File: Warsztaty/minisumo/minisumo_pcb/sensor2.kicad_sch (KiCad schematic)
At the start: 1 part

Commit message: chyba gotowy schemat
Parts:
- removed SPI1: MTSW-103-23-F-D-230, MTSW-103-23-F-D-230:SAMTEC_MTSW-103-23-F-D-230, symbol MTSW-103-23-F-D-230:MTSW-103-23-F-D-230
- added SPI3: MTSW-103-23-F-D-230, MTSW-103-23-F-D-230:SAMTEC_MTSW-103-23-F-D-230, symbol MTSW-103-23-F-D-230:MTSW-103-23-F-D-230
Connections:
- net +5V: now also SPI3.02
- net GND: now also SPI3.01
- new net G2: SPI3.06
- new net SCL: SPI3.04
- new net SDA: SPI3.03
- new net X2: SPI3.05
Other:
- note added: "Sensor2"
- note removed: "Programming connector"

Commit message: stan przed usunięciem jednego czujnika lini
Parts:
- added R3: 20k, Resistor_SMD:R_0805_2012Metric, symbol Device:R_Small
- added R6: 10k, Resistor_SMD:R_0805_2012Metric, symbol Device:R_Small
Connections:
- net GND: now also R3.1
- net X2: now also R3.2, R6.2; no longer SPI3.05
- new net: R6.1, SPI3.05

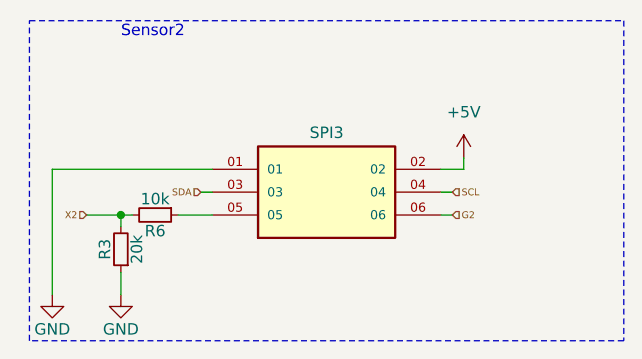
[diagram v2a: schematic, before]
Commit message: Wstępny wyglad robota i płytki
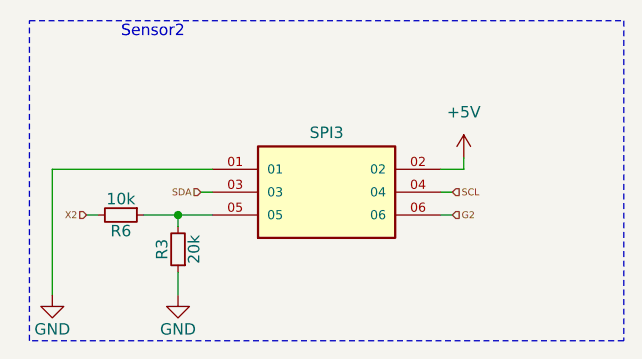
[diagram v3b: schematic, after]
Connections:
- net X2: no longer R3.2
- net at R6.1, SPI3.05: now also R3.2
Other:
- moved on the sheet: R3, R6
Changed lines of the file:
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@@
 	(paper "A4")
 	(junction
-		(at 25.4 35.56)
+		(at 31.75 35.56)
 		(diameter 0)
 		(color 0 0 0 0)
@@
 	(wire
 		(pts
-			(xy 25.4 35.56) (xy 25.4 36.83)
-		)
-		(stroke
-			(width 0)
-			(type default)
-		)
-	)
-	(wire
-		(pts
 			(xy 60.96 33.02) (xy 62.23 33.02)
 		)
@@
 	(wire
 		(pts
-			(xy 25.4 35.56) (xy 26.67 35.56)
-		)
-		(stroke
-			(width 0)
-			(type default)
-		)
-	)
-	(wire
-		(pts
 			(xy 63.5 29.21) (xy 63.5 30.48)
 		)
@@
 	(wire
 		(pts
-			(xy 21.59 35.56) (xy 25.4 35.56)
+			(xy 31.75 35.56) (xy 31.75 36.83)
+		)
+		(stroke
+			(width 0)
+			(type default)
+		)
+	)
+	(wire
+		(pts
+			(xy 21.59 35.56) (xy 22.86 35.56)
+		)
+		(stroke
+			(width 0)
+			(type default)
+		)
+	)
+	(wire
+		(pts
+			(xy 31.75 35.56) (xy 35.56 35.56)
 		)
 		(stroke
@@
 	(wire
 		(pts
-			(xy 31.75 35.56) (xy 35.56 35.56)
+			(xy 27.94 35.56) (xy 31.75 35.56)
 		)
 		(stroke
@@
 	(wire
 		(pts
-			(xy 25.4 41.91) (xy 25.4 44.45)
+			(xy 31.75 41.91) (xy 31.75 44.45)
 		)
 		(stroke
@@
 	(symbol
 		(lib_id "Device:R_Small")
-		(at 29.21 35.56 270)
+		(at 25.4 35.56 270)
 		(unit 1)
 		(exclude_from_sim no)
@@
 		(dnp no)
 		(property "Reference" "R6"
-			(at 29.21 37.338 90)
+			(at 25.4 37.338 90)
 			(effects
 				(font
@@
 		)
 		(property "Value" "10k"
-			(at 29.21 33.782 90)
+			(at 25.4 33.782 90)
 			(effects
 				(font
@@
 		)
 		(property "Footprint" "Resistor_SMD:R_0805_2012Metric"
-			(at 29.21 35.56 0)
+			(at 25.4 35.56 0)
 			(effects
 				(font
@@
 		)
 		(property "Datasheet" "~"
-			(at 29.21 35.56 0)
+			(at 25.4 35.56 0)
 			(effects
 				(font
@@
 		)
 		(property "Description" "Resistor, small symbol"
-			(at 29.21 35.56 0)
+			(at 25.4 35.56 0)
 			(effects
 				(font
@@
 	(symbol
 		(lib_id "power:GND")
-		(at 25.4 44.45 0)
+		(at 31.75 44.45 0)
 		(unit 1)
 		(exclude_from_sim no)
@@
 		(dnp no)
 		(property "Reference" "#PWR030"
-			(at 25.4 50.8 0)
+			(at 31.75 50.8 0)
 			(effects
 				(font
@@
 		)
 		(property "Value" "GND"
-			(at 25.4 48.26 0)
+			(at 31.75 48.26 0)
 			(effects
 				(font
@@
 		)
 		(property "Footprint" ""
-			(at 25.4 44.45 0)
+			(at 31.75 44.45 0)
 			(effects
 				(font
@@
 		)
 		(property "Datasheet" ""
-			(at 25.4 44.45 0)
+			(at 31.75 44.45 0)
 			(effects
 				(font
@@
 		)
 		(property "Description" "Power symbol creates a global label with name \"GND\" , ground"
-			(at 25.4 44.45 0)
+			(at 31.75 44.45 0)
 			(effects
 				(font
@@
 	(symbol
 		(lib_id "Device:R_Small")
-		(at 25.4 39.37 180)
+		(at 31.75 39.37 180)
 		(unit 1)
 		(exclude_from_sim no)
@@
 		(dnp no)
 		(property "Reference" "R3"
-			(at 23.622 39.37 90)
+			(at 29.972 39.37 90)
 			(effects
 				(font
@@
 		)
 		(property "Value" "20k"
-			(at 27.178 39.37 90)
+			(at 33.528 39.37 90)
 			(effects
 				(font
@@
 		)
 		(property "Footprint" "Resistor_SMD:R_0805_2012Metric"
-			(at 25.4 39.37 0)
+			(at 31.75 39.37 0)
 			(effects
 				(font
@@
 		)
 		(property "Datasheet" "~"
-			(at 25.4 39.37 0)
+			(at 31.75 39.37 0)
 			(effects
 				(font
@@
 		)
 		(property "Description" "Resistor, small symbol"
-			(at 25.4 39.37 0)
-			(effects
-				(font
+			(at 31.75 39.37 0)
+			(effects
+				(font

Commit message: koncowy projekt plytki i chyba model tez
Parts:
- renumbered SPI3 to ES2
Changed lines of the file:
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@@
 		(on_board yes)
 		(dnp no)
-		(property "Reference" "SPI3"
+		(property "Reference" "ES2"
 			(at 48.26 26.416 0)
 			(effects
@@
 			(project "minisumo_pcb"
 				(path "/7b99a4ad-c15f-48f5-acdf-b2b295c8ee3b/2ef7160b-0123-47ce-9aa9-4acb05a9135f"
-					(reference "SPI3")
+					(reference "ES2")
 					(unit 1)
 				)

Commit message: prawdopodobnie koncowa wersja płytki
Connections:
- net X2 renamed XSHUT_2
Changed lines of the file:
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@@
 		)
 	)
-	(hierarchical_label "X2"
+	(hierarchical_label "XSHUT_2"
 		(shape input)
 		(at 21.59 35.56 180)
